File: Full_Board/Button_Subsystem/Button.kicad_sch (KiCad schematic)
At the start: 7 parts, among them U6 UCLAMP3301H.TCT

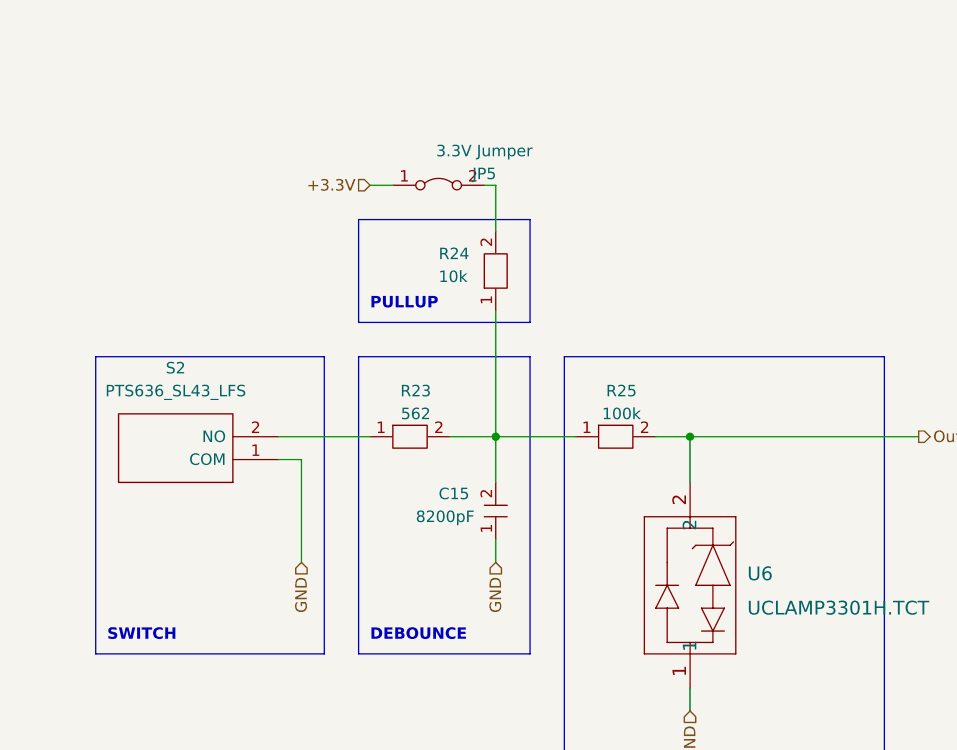
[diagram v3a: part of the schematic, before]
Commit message: Redo pinout, finish pcb layout (no traces)
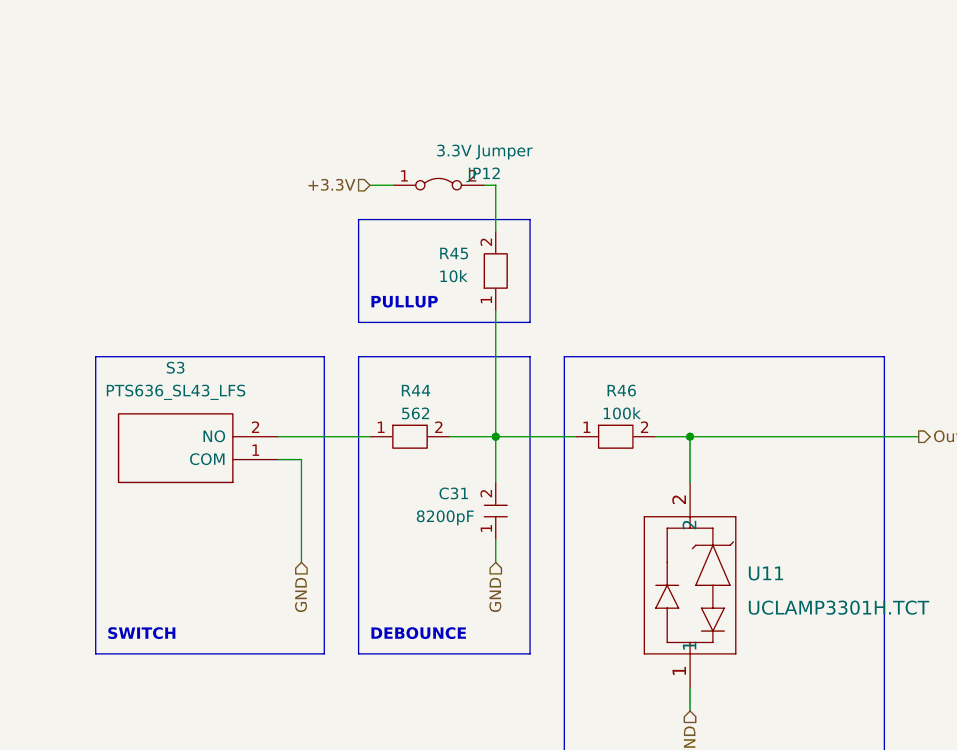
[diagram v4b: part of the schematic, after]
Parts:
- removed C15: 8200pF, C1210C822K2RACAUTO:CAPC3225X88N, symbol C1210C822K2RACAUTO:C1210C822K2RACAUTO
- removed JP5: 3.3V Jumper, TestPoint:TestPoint_2Pads_Pitch2.54mm_Drill0.8mm, symbol Jumper:Jumper_2_Bridged
- removed R23: 562, CR0402-FX-5620GLF:RESC1005X40N, symbol CR0402-FX-5620GLF:CR0402-FX-5620GLF
- removed R24: 10k, RMCF1206FT10K0:RMCF1206FT10K0, symbol RMCF1206FT10K0:10k
- removed R25: 100k, RCV2512100KFKEGAT:RESC6332X70N, symbol RCV2512100KFKEGAT:RCV2512100KFKEGAT
- removed U6: UCLAMP3301H.TCT, UCLAMP3310H-TCT:UCLAMP3301H.TCT, symbol UCLAMP3301H-TCT:UCLAMP3301H.TCT
- added C31: 8200pF, C1210C822K2RACAUTO:CAPC3225X88N, symbol C1210C822K2RACAUTO:C1210C822K2RACAUTO
- added JP12: 3.3V Jumper, TestPoint:TestPoint_2Pads_Pitch2.54mm_Drill0.8mm, symbol Jumper:Jumper_2_Bridged
- added R44: 562, CR0402-FX-5620GLF:RESC1005X40N, symbol CR0402-FX-5620GLF:CR0402-FX-5620GLF
- added R45: 10k, RMCF1206FT10K0:RMCF1206FT10K0, symbol RMCF1206FT10K0:10k
- added R46: 100k, RCV2512100KFKEGAT:RESC6332X70N, symbol RCV2512100KFKEGAT:RCV2512100KFKEGAT
- added U11: UCLAMP3301H.TCT, UCLAMP3310H-TCT:UCLAMP3301H.TCT, symbol UCLAMP3301H-TCT:UCLAMP3301H.TCT
- renumbered S2 to S3
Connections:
- net +3.3V: now also JP12.1 (A)
- net GND: now also C31.1, U11.1
- net Out: now also R46.2, U11.2
- net at S3.2 (NO): now also R44.1
- new net: C31.2, R44.2, R45.1, R46.1
- new net: JP12.2 (B), R45.2

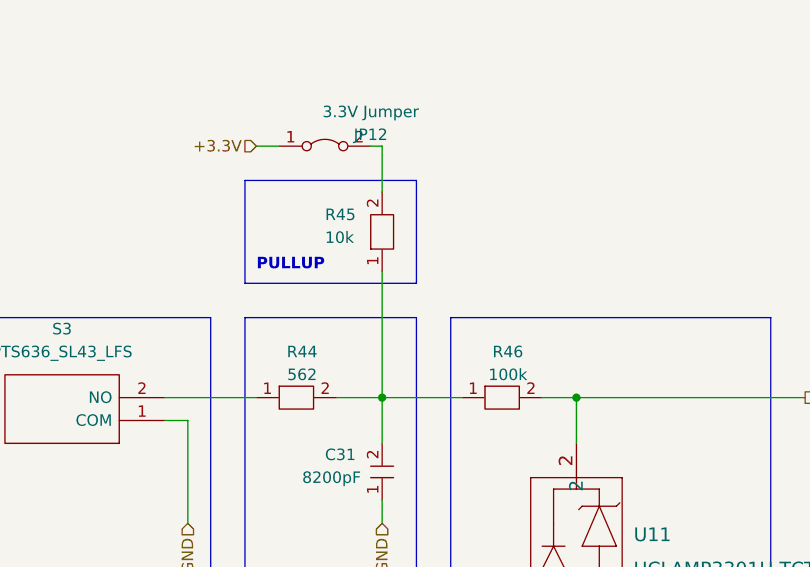
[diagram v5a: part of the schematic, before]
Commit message: Replace small resistors/capacitors with through-hole; fix DRC aside from electromagnet and MUXes
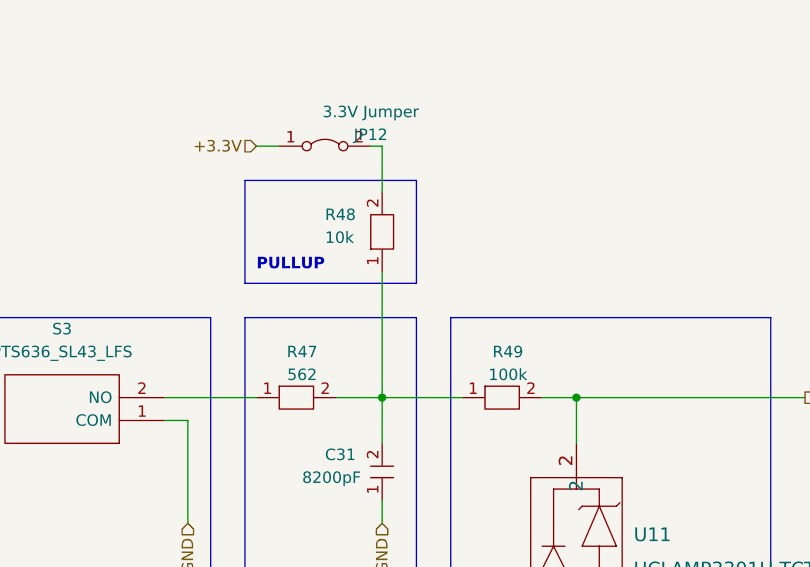
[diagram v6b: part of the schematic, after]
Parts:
- renumbered R44 to R47, R45 to R48, R46 to R49
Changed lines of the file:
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@@
   (symbol (lib_id "RMCF1206FT10K0:10k") (at 137.16 80.01 90) (unit 1)
     (in_bom yes) (on_board yes)
-    (property "Reference" "R45" (id 0) (at 130.81 73.66 90)
+    (property "Reference" "R48" (id 0) (at 130.81 73.66 90)
       (effects (font (size 1.27 1.27)) (justify right))
     )
@@
   (symbol (lib_id "CR0402-FX-5620GLF:CR0402-FX-5620GLF") (at 123.19 93.98 0) (unit 1)
     (in_bom yes) (on_board yes)
-    (property "Reference" "R44" (id 0) (at 128.27 88.9 0))
+    (property "Reference" "R47" (id 0) (at 128.27 88.9 0))
     (property "Value" "562" (id 1) (at 128.27 91.44 0))
     (property "Footprint" "CR0402-FX-5620GLF:RESC1005X40N" (id 2) (at 137.16 92.71 0)
@@
   (symbol (lib_id "RCV2512100KFKEGAT:RCV2512100KFKEGAT") (at 146.05 93.98 0) (unit 1)
     (in_bom yes) (on_board yes)
-    (property "Reference" "R46" (id 0) (at 151.13 88.9 0))
+    (property "Reference" "R49" (id 0) (at 151.13 88.9 0))
     (property "Value" "100k" (id 1) (at 151.13 91.44 0))
     (property "Footprint" "RCV2512100KFKEGAT:RESC6332X70N" (id 2) (at 160.02 92.71 0)

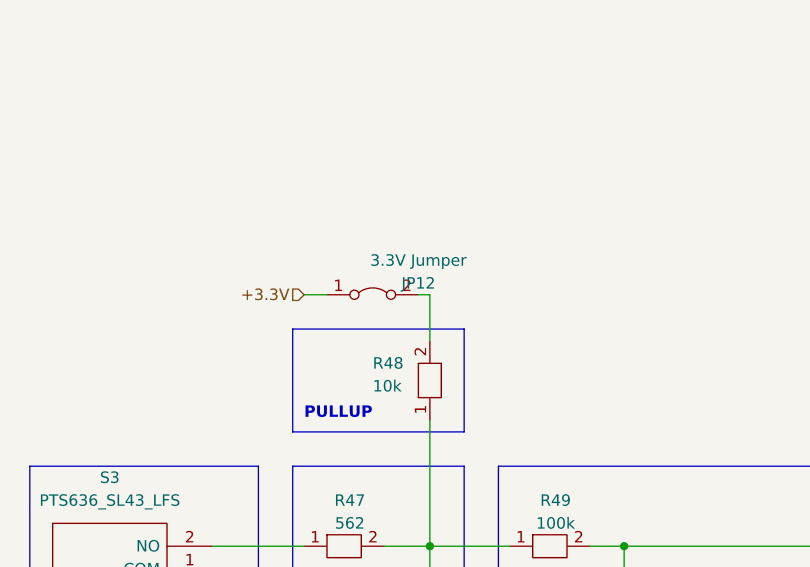
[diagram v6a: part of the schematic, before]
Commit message: Cleanup all schematics and project libs
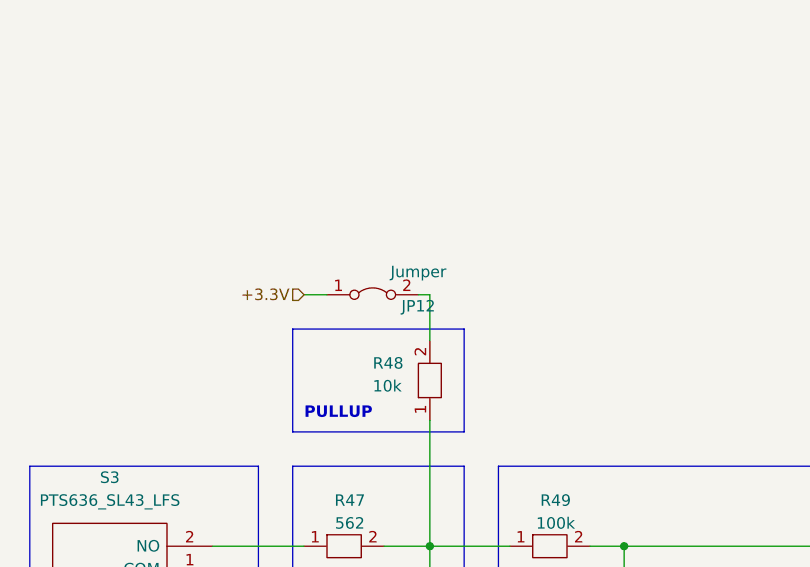
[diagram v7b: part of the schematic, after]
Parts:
- C31: Digikey Link (none) -> https://www.digikey.com/en/products/detail/kemet/C1210C822K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; Digikey link https://www.digikey.com/en/products/detail/kemet/C1210C822K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 -> (none); Mouser Link (none) -> https://www.mouser.com/ProductDetail/KEMET/C1210C822K2RACAU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; Mouser link https://www.mouser.com/ProductDetail/KEMET/C1210C822K2RACAU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 -> (none)
- JP12: value 3.3V Jumper -> Jumper; symbol Jumper:Jumper_2_Bridged -> PH1-02-UA:PH1-02-UA; Digikey Link https://www.digikey.com/en/products/detail/adam-tech/PH1-02-UA/9830266 -> https://www.digikey.com/en/products/detail/adam-tech/PH1-02-UA/9830266?s=N4IgTCBcDa4AwFYDsBaACgCQIwrmFAqgIIoByAIiALoC%2BQA; Manufacturer's Part Number (none) -> PH1-02-UA; Manufacturers Part Number PH1-02-UA -> (none)
- R47: Digikey Link (none) -> https://www.digikey.com/en/products/detail/bourns-inc/CR040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; Digikey link https://www.digikey.com/en/products/detail/bourns-inc/CR040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 -> (none); Mouse link https://www.mouser.com/ProductDetail/Bourns/CR0402-FX-5620G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 -> (none); Mouser Link (none) -> https://www.mouser.com/ProductDetail/Bourns/CR0402-FX-5620G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
- R48: Digikey Link (none) -> https://www.digikey.com/en/products/detail/stackpole-electr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; Digikey link https://www.digikey.com/en/products/detail/stackpole-electr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 -> (none)
- R49: Digikey Link (none) -> https://www.digikey.com/en/products/detail/vishay-dale/RCV2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; Digikey link https://www.digikey.com/en/products/detail/vishay-dale/RCV2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 -> (none); Mouser Link (none) -> https://www.mouser.com/ProductDetail/Vishay-Draloric/RCV251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; Mouser link https://www.mouser.com/ProductDetail/Vishay-Draloric/RCV251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 -> (none)
- S3: Digikey Link (none) -> https://www.digikey.com/en/products/detail/c-k/PTS636-SL43-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; Digikey link https://www.digikey.com/en/products/detail/c-k/PTS636-SL43-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 -> (none); Mouser Link (none) -> https://www.mouser.com/ProductDetail/CK/PTS636-SL43-LFS?qs=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; Mouser link https://www.mouser.com/ProductDetail/CK/PTS636-SL43-LFS?qs=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 -> (none); Mouser link  https://www.mouser.com/ProductDetail/CK/PTS636-SL43-LFS?qs=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 -> (none)
- U11: Manufacturer's Part Number (none) -> UCLAMP3301H.TCT; Manufacturers Part Number UCLAMP3301H.TCT -> (none); Mouser Link (none) -> https://www.mouser.com/ProductDetail/Semtech/UCLAMP3301H.TC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; Mouser Part Number (none) -> 947-UCLAMP3301H.TCT
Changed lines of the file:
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@@
       (effects (font (size 1.27 1.27)) (justify left) hide)
     )
-    (property "Digikey link" "https://www.digikey.com/en/products/detail/stackpole-electronics-inc/RMCF1206FT10K0/1759669" (id 7) (at 148.59 66.04 0)
+    (property "Digikey Link" "https://www.digikey.com/en/products/detail/stackpole-electronics-inc/RMCF1206FT10K0/1759669" (id 7) (at 148.59 66.04 0)
       (effects (font (size 1.27 1.27)) (justify left) hide)
     )
-    (property "Mouser link" "" (id 8) (at 151.13 66.04 0)
+    (property "Mouser Link" "" (id 8) (at 151.13 66.04 0)
       (effects (font (size 1.27 1.27)) (justify left) hide)
     )
@@
     (pin "2")
   )
-  (symbol (lib_id "Jumper:Jumper_2_Bridged") (at 130.81 66.04 0) (unit 1)
+  (symbol (lib_id "PH1-02-UA:PH1-02-UA") (at 130.81 68.58 0) (unit 1)
     (in_bom yes) (on_board yes)
-    (property "Reference" "JP12" (id 0) (at 135.89 64.77 0))
-    (property "Value" "3.3V Jumper" (id 1) (at 135.89 62.23 0))
-    (property "Footprint" "TestPoint:TestPoint_2Pads_Pitch2.54mm_Drill0.8mm" (id 2) (at 130.81 66.04 0)
+    (property "Reference" "JP12" (id 0) (at 135.89 67.31 0))
+    (property "Value" "Jumper" (id 1) (at 135.89 63.5 0))
+    (property "Footprint" "TestPoint:TestPoint_2Pads_Pitch2.54mm_Drill0.8mm" (id 2) (at 130.81 68.58 0)
       (effects (font (size 1.27 1.27)) hide)
     )
-    (property "Datasheet" "~" (id 3) (at 130.81 66.04 0)
+    (property "Datasheet" "https://app.adam-tech.com/products/download/data_sheet/201605/ph1-xx-ua-data-sheet.pdf" (id 3) (at 130.81 68.58 0)
       (effects (font (size 1.27 1.27)) hide)
     )
-    (property "Manufacturers Part Number" "PH1-02-UA" (id 4) (at 130.81 66.04 0)
+    (property "Digikey Part Number" "2057-PH1-02-UA-ND" (id 5) (at 130.81 68.58 0)
       (effects (font (size 1.27 1.27)) hide)
     )
-    (property "Digikey Part Number" "2057-PH1-02-UA-ND" (id 5) (at 130.81 66.04 0)
+    (property "Mouser Part Number" "" (id 6) (at 130.81 68.58 0)
       (effects (font (size 1.27 1.27)) hide)
     )
-    (property "Mouser Part Number" "" (id 6) (at 130.81 66.04 0)
+    (property "Digikey Link" "https://www.digikey.com/en/products/detail/adam-tech/PH1-02-UA/9830266?s=N4IgTCBcDa4AwFYDsBaACgCQIwrmFAqgIIoByAIiALoC%2BQA" (id 7) (at 130.81 68.58 0)
       (effects (font (size 1.27 1.27)) hide)
     )
-    (property "Digikey Link" "https://www.digikey.com/en/products/detail/adam-tech/PH1-02-UA/9830266" (id 7) (at 130.81 66.04 0)
+    (property "Mouser Link" "" (id 8) (at 130.81 68.58 0)
       (effects (font (size 1.27 1.27)) hide)
     )
-    (property "Mouser Link" "" (id 8) (at 130.81 66.04 0)
+    (property "Manufacturer's Part Number" "PH1-02-UA" (id 9) (at 130.81 68.58 0)
       (effects (font (size 1.27 1.27)) hide)
     )
@@
       (effects (font (size 1.27 1.27)) (justify left) hide)
     )
-    (property "Digikey link" "https://www.digikey.com/en/products/detail/bourns-inc/CR0402-FX-5620GLF/3783429?s=N4IgTCBcDaIAQGEBKAGALCsBaAYgDSwFYA2MFAcQBkcQBdAXyA" (id 7) (at 137.16 105.41 0)
+    (property "Digikey Link" "https://www.digikey.com/en/products/detail/bourns-inc/CR0402-FX-5620GLF/3783429?s=N4IgTCBcDaIAQGEBKAGALCsBaAYgDSwFYA2MFAcQBkcQBdAXyA" (id 7) (at 137.16 105.41 0)
       (effects (font (size 1.27 1.27)) (justify left) hide)
     )
-    (property "Mouse link" "https://www.mouser.com/ProductDetail/Bourns/CR0402-FX-5620GLF?qs=sGAEpiMZZMtlubZbdhIBIDfFWzqdPB9%252B4rUQL12%252Bb9s%3D" (id 8) (at 137.16 107.95 0)
+    (property "Mouser Link" "https://www.mouser.com/ProductDetail/Bourns/CR0402-FX-5620GLF?qs=sGAEpiMZZMtlubZbdhIBIDfFWzqdPB9%252B4rUQL12%252Bb9s%3D" (id 8) (at 137.16 107.95 0)
       (effects (font (size 1.27 1.27)) (justify left) hide)
     )
@@
       (effects (font (size 1.524 1.524)) hide)
     )
-    (property "Manufacturers Part Number" "UCLAMP3301H.TCT" (id 4) (at 158.75 130.81 0)
-      (effects (font (size 1.27 1.27)) hide)
-    )
     (property "Digikey Part Number" "UCLAMP3301HDKR-ND" (id 5) (at 158.75 130.81 0)
       (effects (font (size 1.27 1.27)) hide)
     )
-    (property "Mouser Part Number" "" (id 6) (at 158.75 130.81 0)
+    (property "Mouser Part Number" " 947-UCLAMP3301H.TCT " (id 6) (at 158.75 130.81 0)
       (effects (font (size 1.27 1.27)) hide)
     )
@@
       (effects (font (size 1.27 1.27)) hide)
     )
-    (property "Mouser Link" "" (id 8) (at 158.75 130.81 0)
+    (property "Mouser Link" "https://www.mouser.com/ProductDetail/Semtech/UCLAMP3301H.TCT?qs=rBWM4%252BvDhIeimYmappCp5Q%3D%3D" (id 8) (at 158.75 130.81 0)
+      (effects (font (size 1.27 1.27)) hide)
+    )
+    (property "Manufacturer's Part Number" "UCLAMP3301H.TCT" (id 9) (at 158.75 130.81 0)
       (effects (font (size 1.27 1.27)) hide)
     )
@@
       (effects (font (size 1.27 1.27)) (justify left) hide)
     )
-    (property "Digikey link" "https://www.digikey.com/en/products/detail/vishay-dale/RCV2512100KFKEGAT/13985179?s=N4IgTCBcDaIEoGEBqYCsBGM6AM2DSAYngKIDiAggCoAEIAugL5A" (id 7) (at 160.02 107.95 0)
+    (property "Digikey Link" "https://www.digikey.com/en/products/detail/vishay-dale/RCV2512100KFKEGAT/13985179?s=N4IgTCBcDaIEoGEBqYCsBGM6AM2DSAYngKIDiAggCoAEIAugL5A" (id 7) (at 160.02 107.95 0)
       (effects (font (size 1.27 1.27)) (justify left) hide)
     )
-    (property "Mouser link" "https://www.mouser.com/ProductDetail/Vishay-Draloric/RCV2512100KFKEGAT?qs=sGAEpiMZZMtlubZbdhIBIOK8YY79HZuiqCZ6uF64pjM%3D" (id 8) (at 160.02 105.41 0)
+    (property "Mouser Link" "https://www.mouser.com/ProductDetail/Vishay-Draloric/RCV2512100KFKEGAT?qs=sGAEpiMZZMtlubZbdhIBIOK8YY79HZuiqCZ6uF64pjM%3D" (id 8) (at 160.02 105.41 0)
       (effects (font (size 1.27 1.27)) (justify left) hide)
     )
@@
       (effects (font (size 1.27 1.27)) (justify left) hide)
     )
-    (property "Digikey link" "https://www.digikey.com/en/products/detail/c-k/PTS636-SL43-LFS/10071714" (id 7) (at 93.98 91.44 0)
+    (property "Digikey Link" "https://www.digikey.com/en/products/detail/c-k/PTS636-SL43-LFS/10071714" (id 7) (at 93.98 91.44 0)
       (effects (font (size 1.27 1.27)) (justify left) hide)
     )
-    (property "Mouser link" "https://www.mouser.com/ProductDetail/CK/PTS636-SL43-LFS?qs=vLWxofP3U2xHB0Q2opWSaw%3D%3D" (id 8) (at 93.98 86.36 0)
-      (effects (font (size 1.27 1.27)) (justify left) hide)
-    )
-    (property "Mouser link " "https://www.mouser.com/ProductDetail/CK/PTS636-SL43-LFS?qs=vLWxofP3U2xHB0Q2opWSaw%3D%3D" (id 9) (at 93.98 86.36 0)
+    (property "Mouser Link" "https://www.mouser.com/ProductDetail/CK/PTS636-SL43-LFS?qs=vLWxofP3U2xHB0Q2opWSaw%3D%3D" (id 8) (at 93.98 86.36 0)
       (effects (font (size 1.27 1.27)) (justify left) hide)
     )
@@
       (effects (font (size 1.27 1.27)) (justify left) hide)
     )
-    (property "Digikey link" "https://www.digikey.com/en/products/detail/kemet/C1210C822K2RACAUTO/16524786?s=N4IgTCBcDaIMIEYwIAxwBxjAaTAJQEE4CBVAFQHkACEAXQF8g" (id 7) (at 148.59 96.52 0)
+    (property "Digikey Link" "https://www.digikey.com/en/products/detail/kemet/C1210C822K2RACAUTO/16524786?s=N4IgTCBcDaIMIEYwIAxwBxjAaTAJQEE4CBVAFQHkACEAXQF8g" (id 7) (at 148.59 96.52 0)
       (effects (font (size 1.27 1.27)) (justify left) hide)
     )
-    (property "Mouser link" "https://www.mouser.com/ProductDetail/KEMET/C1210C822K2RACAUTO?qs=sGAEpiMZZMukHu%252BjC5l7YfRfrXj%2FJXIdfvr9FKYreLc%3D" (id 8) (at 151.13 96.52 0)
+    (property "Mouser Link" "https://www.mouser.com/ProductDetail/KEMET/C1210C822K2RACAUTO?qs=sGAEpiMZZMukHu%252BjC5l7YfRfrXj%2FJXIdfvr9FKYreLc%3D" (id 8) (at 151.13 96.52 0)
       (effects (font (size 1.27 1.27)) (justify left) hide)
     )
